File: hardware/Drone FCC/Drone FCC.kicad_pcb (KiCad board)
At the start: 2 copper layers, 137.2 x 68.6 mm, 24 parts, among them J1 Mag Dupont, J17 Conn_01x04, J18 Conn_01x04, J19 GPS M8N - DF13, J2 GPS Dupont, J20 Mag DF13, J21 Micro_SD_Card_Det_Hirose_DM3AT, J22 Conn_02x05_Odd_Even, J23 47589-0001, J24 DSM Spektrum JST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

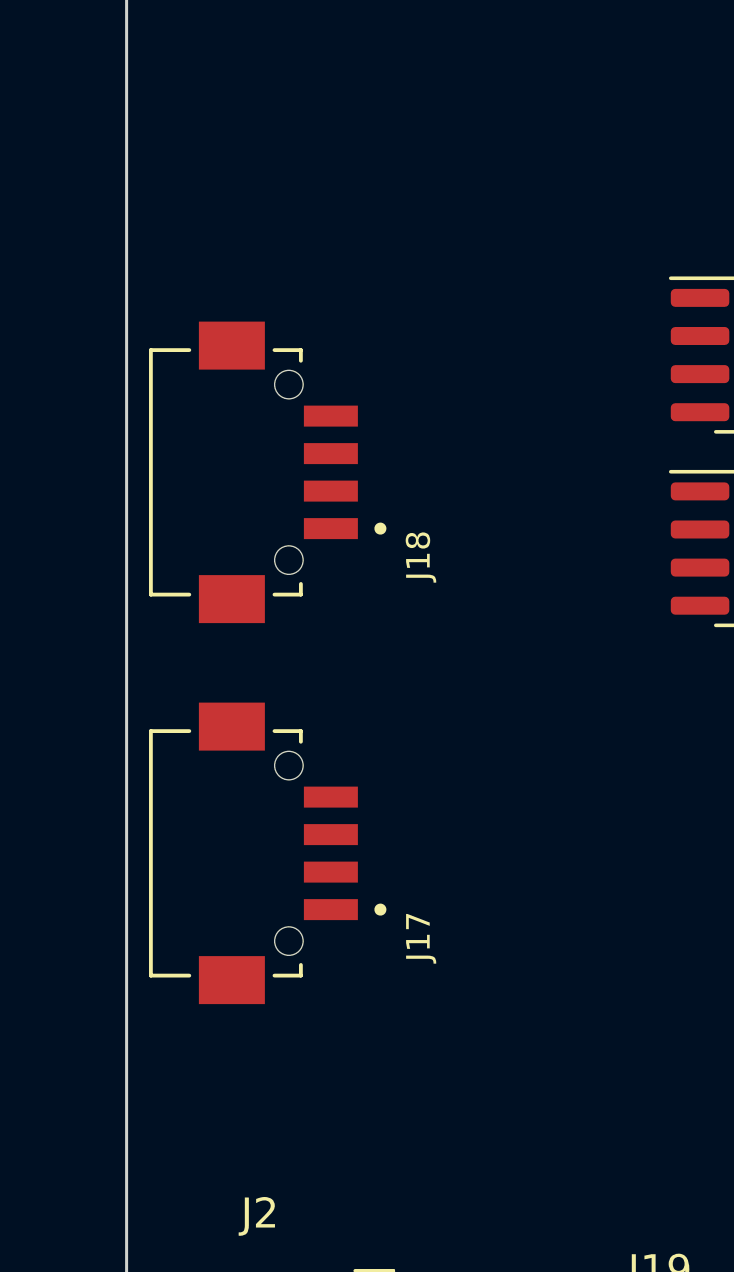
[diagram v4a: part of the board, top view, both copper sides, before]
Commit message: add functional schematic for microSD
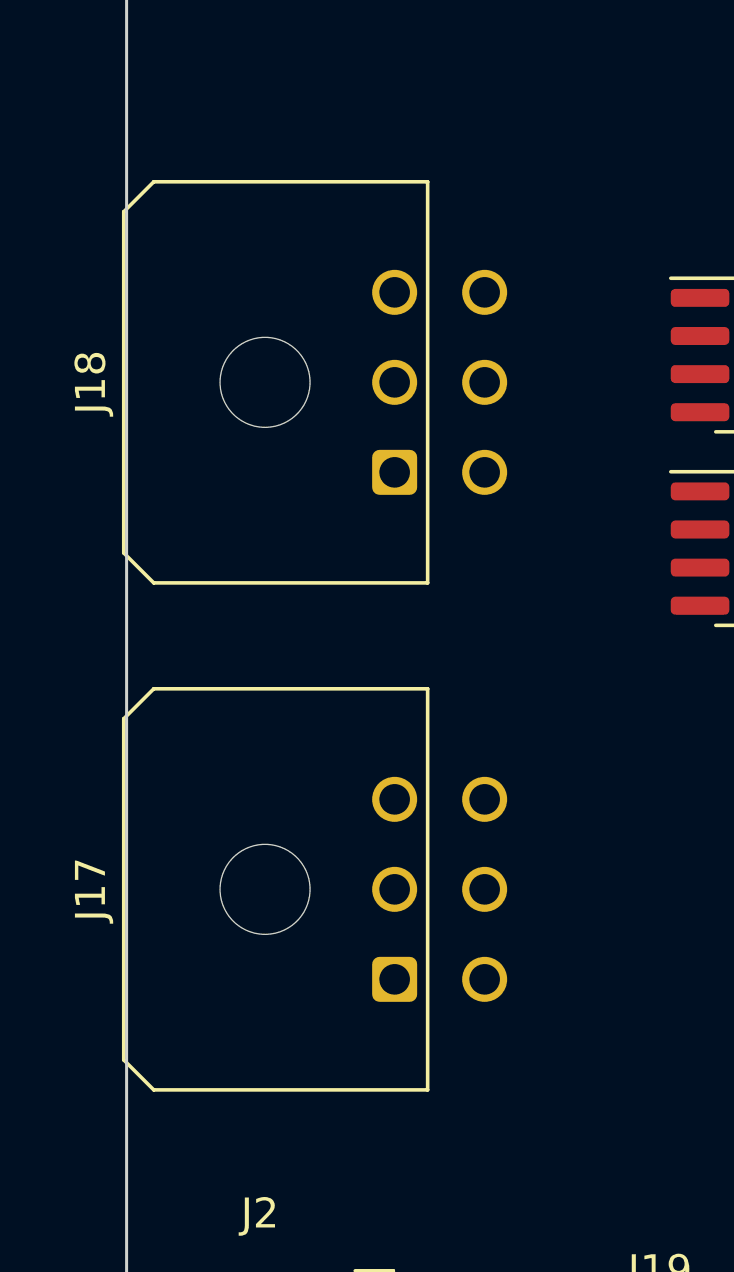
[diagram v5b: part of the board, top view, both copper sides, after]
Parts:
- J17: value Conn_01x04 -> CAN 1; footprint DF13-4P-1.25H:HRS_DF13-4P-1.25H(75) -> Connector_Molex:Molex_Micro-Fit_3.0_43045-0600_2x03_P3.00mm_Horizontal
- J18: value Conn_01x04 -> CAN 2; footprint DF13-4P-1.25H:HRS_DF13-4P-1.25H(75) -> Connector_Molex:Molex_Micro-Fit_3.0_43045-0600_2x03_P3.00mm_Horizontal
- moved J17 5.48 mm to (91.5, 82.9)
- moved J18 3.53 mm to (91.5, 66.0)
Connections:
- J17 pad 1: 5V -> unconnected-(J17-Pad1)
- J17 pad 4: GND -> unconnected-(J17-Pad4)
- J18 pad 1: 5V -> unconnected-(J18-Pad1)
- J18 pad 4: GND -> unconnected-(J18-Pad4)

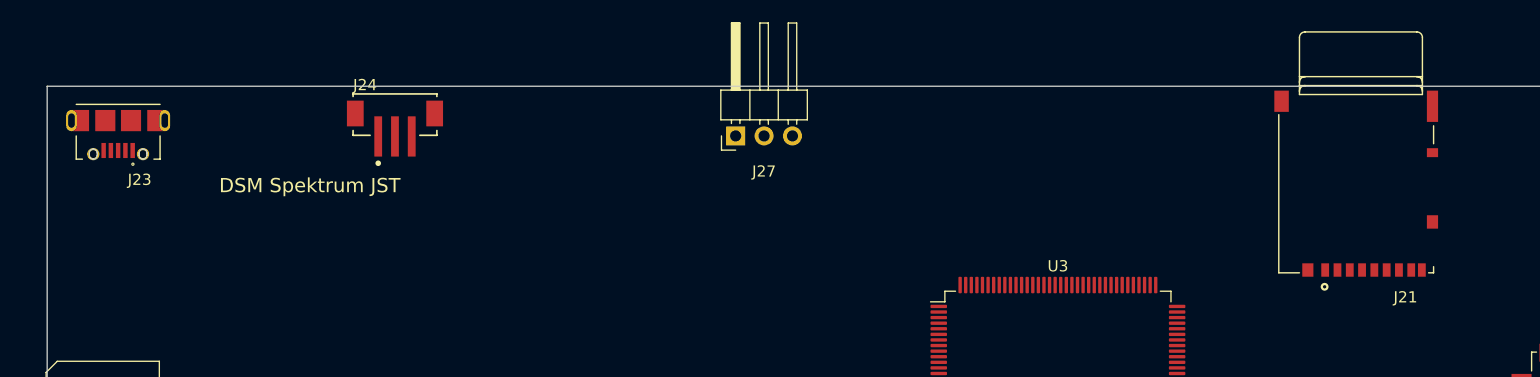
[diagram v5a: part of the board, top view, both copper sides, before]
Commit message: changed usb 2.0 AB connector for usb 2.0 B
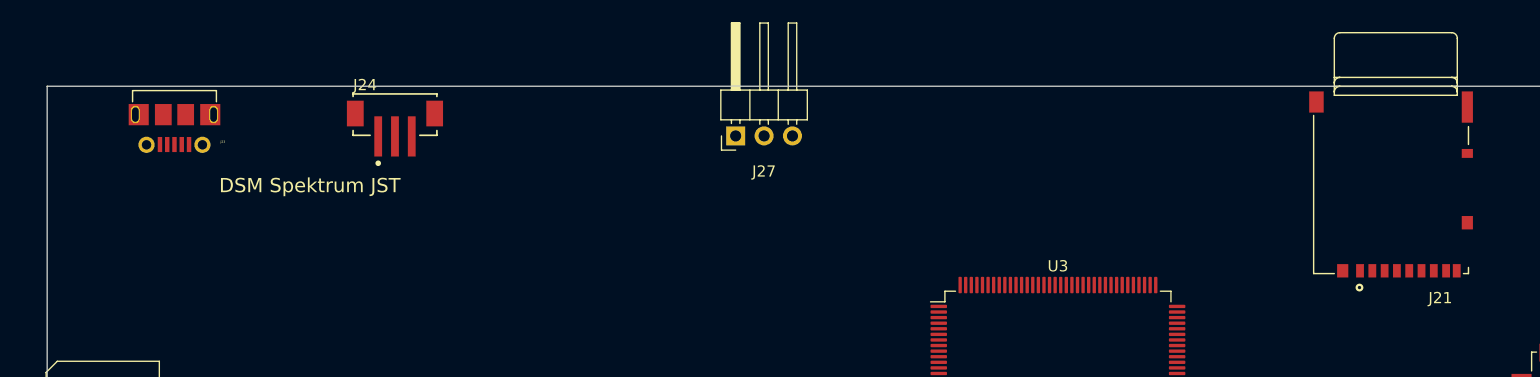
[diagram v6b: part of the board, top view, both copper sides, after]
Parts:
- J23: value 47589-0001 -> 105017-0001; footprint 47589-0001:MOLEX_47589-0001 -> 105017-0001:MOLEX_105017-0001
- moved J23 5.20 mm to (93.9, 34.3)
- moved J21 3.12 mm to (203.2, 48.3)
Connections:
- J21 pad 1: unconnected-(J21-Pad1) -> /MCU/SDMMC1_D2
- J21 pad 2: unconnected-(J21-Pad2) -> /MCU/SDMMC1_D3
- J21 pad 3: unconnected-(J21-Pad3) -> /MCU/SDMMC1_CMD
- J21 pad 5: unconnected-(J21-Pad5) -> /MCU/SDMMC1_CK
- J21 pad 7: unconnected-(J21-Pad7) -> /MCU/SDMMC1_D0
- J21 pad 8: unconnected-(J21-Pad8) -> /MCU/SDMMC1_D1
- U3 pad 111: unconnected-(U3-Pad111) -> /MCU/SDMMC1_D2
- U3 pad 112: unconnected-(U3-Pad112) -> /MCU/SDMMC1_D3
- U3 pad 113: unconnected-(U3-Pad113) -> /MCU/SDMMC1_CK
- U3 pad 116: unconnected-(U3-Pad116) -> /MCU/SDMMC1_CMD
- U3 pad 98: unconnected-(U3-Pad98) -> /MCU/SDMMC1_D0
- U3 pad 99: unconnected-(U3-Pad99) -> /MCU/SDMMC1_D1

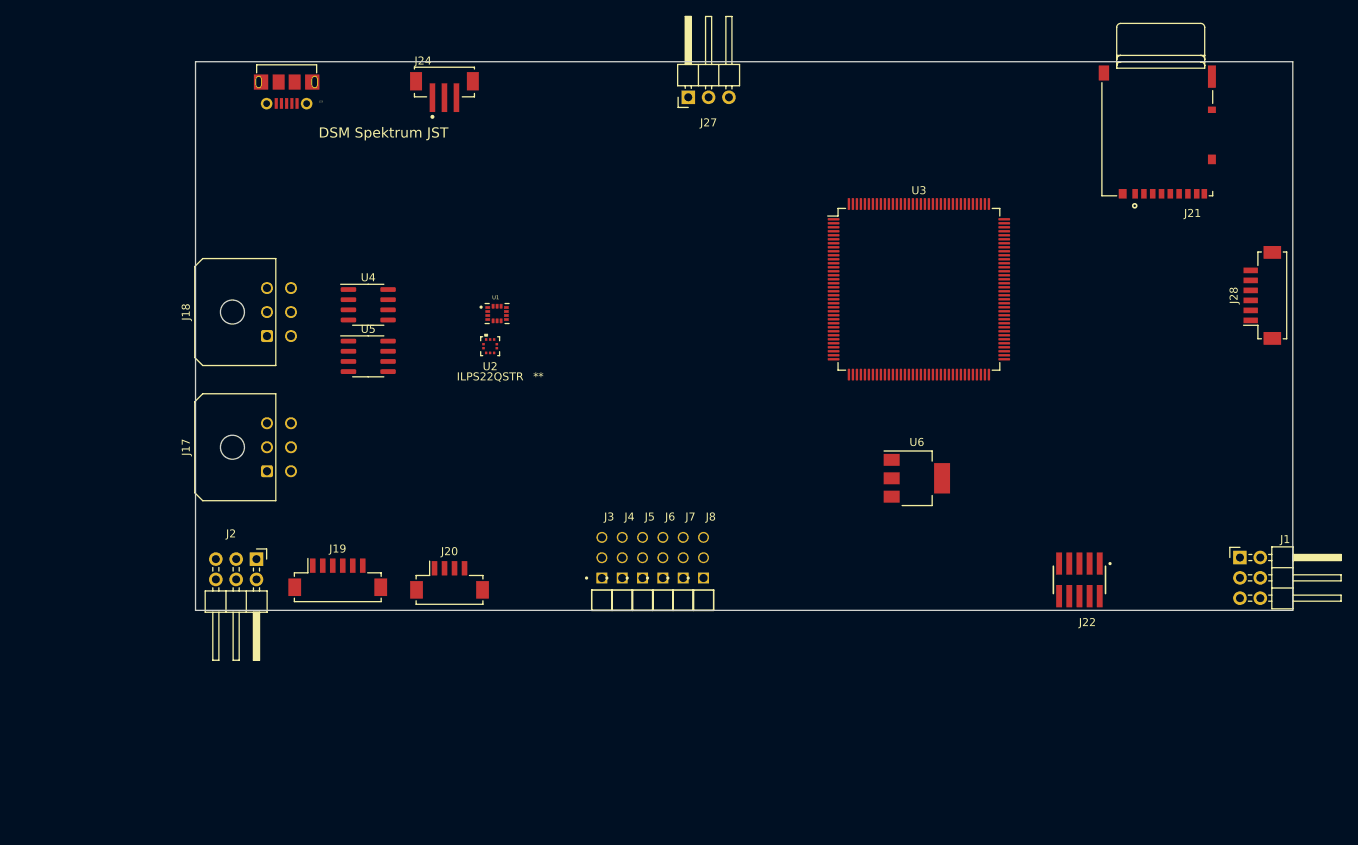
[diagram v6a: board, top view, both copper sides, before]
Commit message: add CAN schematic
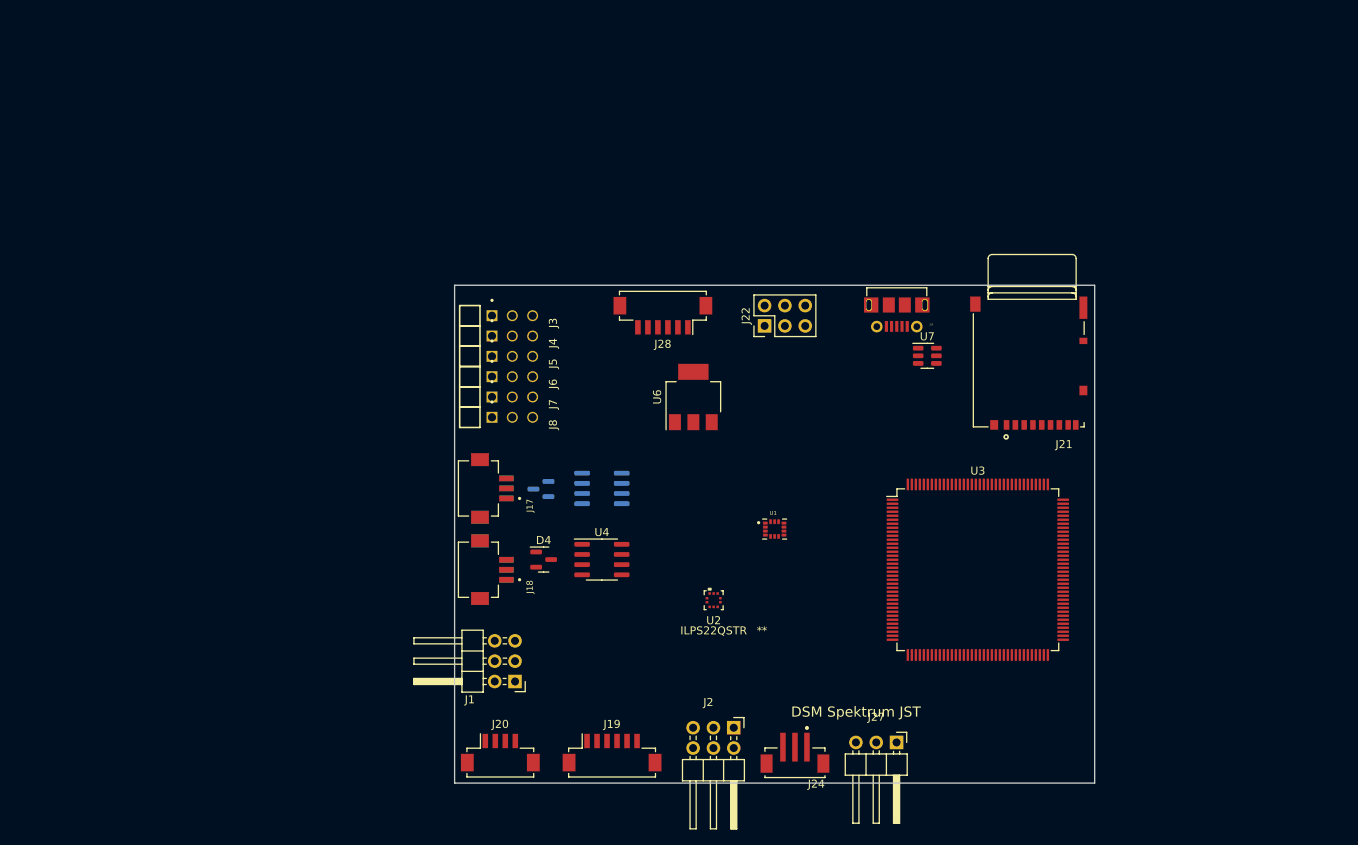
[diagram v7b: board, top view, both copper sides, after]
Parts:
- added D4: SM712_SOT23, Package_TO_SOT_SMD:SOT-23, F.Cu at (126.1, 94.0)
- added D5: SM712_SOT23, Package_TO_SOT_SMD:SOT-23, B.Cu at (125.7, 85.2)
- added J25: 105017-0001, 105017-0001:MOLEX_105017-0001, F.Cu at (170.2, 62.2)
- added J26: Conn_01x03, DF13A-3P-1.25H(21):HRS_DF13A-3P-1.25H(21), B.Cu at (118.1, 95.2)
- added U7: USBLC6-2SC6, Package_TO_SOT_SMD:SOT-23-6, F.Cu at (174.0, 68.5)
- J17: value CAN 1 -> Conn_01x03; footprint Connector_Molex:Molex_Micro-Fit_3.0_43045-0600_2x03_P3.00mm_Horizontal -> DF13A-3P-1.25H(21):HRS_DF13A-3P-1.25H(21)
- J18: value CAN 2 -> Conn_01x03; footprint Connector_Molex:Molex_Micro-Fit_3.0_43045-0600_2x03_P3.00mm_Horizontal -> DF13A-3P-1.25H(21):HRS_DF13A-3P-1.25H(21)
- J22: value Conn_02x05_Odd_Even -> Conn_02x03_Counter_Clockwise; footprint FTSH-105-01-F-DV-K-TR:SAMTEC_FTSH-105-01-F-DV-P-TR -> Connector_PinHeader_2.54mm:PinHeader_2x03_P2.54mm_Vertical
- J23: value 105017-0001 -> Conn_01x03; footprint 105017-0001:MOLEX_105017-0001 -> DF13A-3P-1.25H(21):HRS_DF13A-3P-1.25H(21); moved to B.Cu
- U5: moved to B.Cu
- moved J24 95.7 mm to (157.5, 119.4), turned to 180 degrees
- moved J1 91.9 mm to (122.5, 109.2), turned to 180 degrees
- moved J27 84.7 mm to (170.2, 116.8), turned to -90 degrees
- moved J28 75.0 mm to (141.0, 63.5), turned to 180 degrees
- moved J2 63.3 mm to (149.8, 115.0)
- moved J23 56.3 mm to (118.1, 85.1), turned to -90 degrees
- moved J22 50.6 mm to (153.7, 64.8), turned to 90 degrees
- moved U1 43.9 mm to (154.9, 90.2)
- moved U4 43.2 mm to (133.3, 94.0)
- moved U2 42.3 mm to (147.3, 99.1)
- moved J19 40.7 mm to (134.6, 118.1)
- moved J18 39.5 mm to (118.1, 95.2)
- moved J3 39.2 mm to (116.8, 63.5), turned to -90 degrees
- moved J4 38.1 mm to (116.8, 66.0), turned to -90 degrees
- moved J5 37.4 mm to (116.8, 68.6), turned to -90 degrees
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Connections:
- net /MCU/CAN1_RX renamed /Interfaz_CAN/CAN1_RX
- net /MCU/CAN1_TX renamed /Interfaz_CAN/CAN1_TX
- net /MCU/CAN2_RX renamed /Interfaz_CAN/CAN2_RX
- net /MCU/CAN2_TX renamed /Interfaz_CAN/CAN2_TX
- net /SPI1_MISO renamed /MCU/SPI1_MISO
- net /SPI1_MOSI renamed /MCU/SPI1_MOSI
- net /SPI1_SCK renamed /MCU/SPI1_SCK
- J1 pad 5: /I2C4_SCL -> /Sensores/MAG_SCL
- J1 pad 6: /I2C4_SDA -> /Sensores/MAG_SDA
- J17 pad 1: unconnected-(J17-Pad1) -> Net-(U4-Pad7)
- J17 pad 2: Net-(J17-Pad2) -> Net-(U4-Pad6)
- J17 pad 3: Net-(J17-Pad3) -> GND
- J18 pad 1: unconnected-(J18-Pad1) -> Net-(U4-Pad7)
- J18 pad 2: Net-(J18-Pad2) -> Net-(U4-Pad6)
- J18 pad 3: Net-(J18-Pad3) -> GND
- J19 pad 4: /USART1_RX -> /Sensores/GNSS_Rx
- J19 pad 5: /USART1_TX -> /Sensores/GNSS_Tx
- J2 pad 1: /USART1_TX -> /Sensores/GNSS_Tx
- J2 pad 2: /USART1_RX -> /Sensores/GNSS_Rx
- J20 pad 2: /I2C4_SCL -> /Sensores/MAG_SCL
- J20 pad 3: /I2C4_SDA -> /Sensores/MAG_SDA
- J22 pad 2: /Debug/SWDIO/TMS -> /Debug/SWCLK
- J22 pad 4: /Debug/SWDCLK/TCK -> /Debug/SWDIO
- J22 pad 5: GND -> /Debug/NRST
- J22 pad 6: /Debug/SWO/TDO -> /Debug/SWO
- J23 pad 1: unconnected-(J23-Pad1) -> Net-(D5-Pad1)
- J23 pad 2: unconnected-(J23-Pad2) -> Net-(D5-Pad2)
- J23 pad 3: unconnected-(J23-Pad3) -> GND
- J28 pad 3: unconnected-(J28-Pad3) -> Net-(C9-Pad1)
- J28 pad 4: unconnected-(J28-Pad4) -> Net-(C11-Pad1)
- J3 pad 1: /PWM1 -> /MCU/PWM1
- J4 pad 1: /PWM2 -> /MCU/PWM2
- J5 pad 1: /PWM3 -> /MCU/PWM3
- J6 pad 1: /PWM4 -> /MCU/PWM4
- J7 pad 1: /PWM5 -> /MCU/PWM8
- J8 pad 1: /PWM6 -> /MCU/PWM9
- U2 pad 2: /I2C2_SCL -> /MCU/I2C2_SCL
- U2 pad 4: /I2C2_SDA -> /MCU/I2C2_SDA
- U3 pad 101: /USART1_TX -> /MCU/OTG_FS_VBUS
- U3 pad 102: /USART1_RX -> /MCU/OTG_FS_ID
- U3 pad 103: unconnected-(U3-Pad103) -> /MCU/OTG_FS_DM
- U3 pad 104: unconnected-(U3-Pad104) -> /MCU/OTG_FS_DP
- U3 pad 105: unconnected-(U3-Pad105) -> /Debug/SWDIO
- U3 pad 109: unconnected-(U3-Pad109) -> /Debug/SWCLK
- U3 pad 133: unconnected-(U3-Pad133) -> /Debug/SWO
- U3 pad 23: unconnected-(U3-Pad23) -> /MCU/OSC_IN
- U3 pad 24: unconnected-(U3-Pad24) -> /MCU/OSC_OUT
- U3 pad 25: unconnected-(U3-Pad25) -> /Debug/NRST
- U3 pad 54: /I2C4_SDA -> /Sensores/MAG_SCL
- U3 pad 55: /I2C4_SCL -> /Sensores/MAG_SDA
- U3 pad 69: /I2C2_SDA -> /MCU/I2C2_SCL
- U3 pad 70: /I2C2_SCL -> /MCU/I2C2_SDA
- U3 pad 8: unconnected-(U3-Pad8) -> /MCU/OSC32_IN
- U3 pad 9: unconnected-(U3-Pad9) -> /MCU/OSC32_OUT
- U3 pad 95: unconnected-(U3-Pad95) -> /MCU/VDDUSB
- U4 pad 1: unconnected-(U4-Pad1) -> Net-(U4-Pad1)
- U4 pad 4: unconnected-(U4-Pad4) -> Net-(U4-Pad4)
- U4 pad 6: Net-(J17-Pad3) -> Net-(U4-Pad6)
- U4 pad 7: Net-(J17-Pad2) -> Net-(U4-Pad7)
- U4 pad 8: unconnected-(U4-Pad8) -> Net-(U4-Pad8)
- U5 pad 1: unconnected-(U5-Pad1) -> Net-(R24-Pad2)
- U5 pad 4: unconnected-(U5-Pad4) -> Net-(R21-Pad2)
- U5 pad 6: Net-(J18-Pad3) -> Net-(D5-Pad2)
- U5 pad 7: Net-(J18-Pad2) -> Net-(D5-Pad1)
- U5 pad 8: unconnected-(U5-Pad8) -> Net-(R25-Pad2)
- U6 pad 1: unconnected-(U6-Pad1) -> GND
- U6 pad 2: unconnected-(U6-Pad2) -> 3V3
- U6 pad 3: unconnected-(U6-Pad3) -> Net-(C13-Pad1)
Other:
- board size 137.2 x 68.6 mm -> 80 x 62.2 mm

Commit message: rearranged FCC schematic
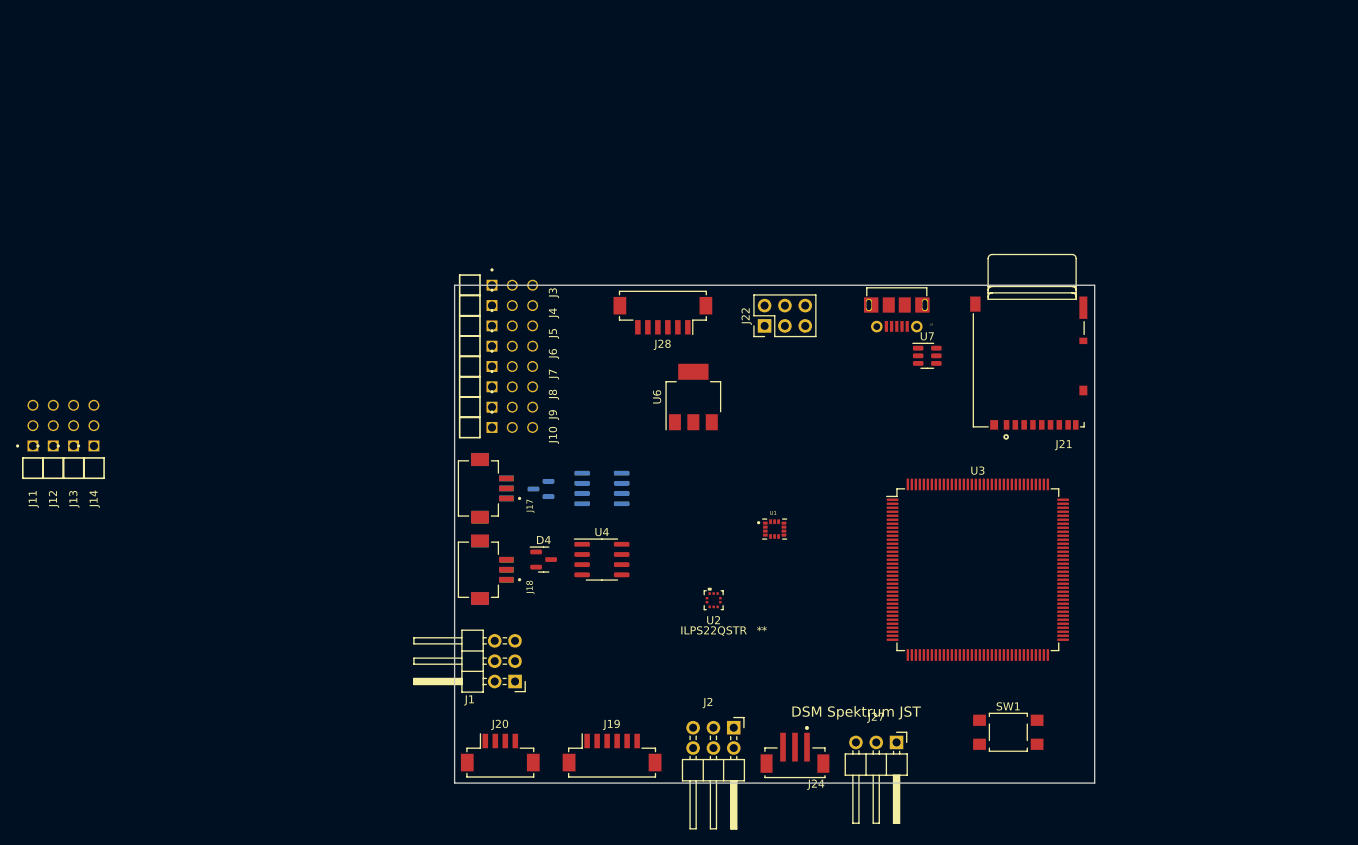
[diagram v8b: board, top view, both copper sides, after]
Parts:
- added J10: Conn_01x03, TSW-101-08-G-T-RA:SAMTEC_TSW-101-08-G-T-RA, F.Cu at (116.8, 77.5)
- added J11: Conn_01x03, TSW-101-08-G-T-RA:SAMTEC_TSW-101-08-G-T-RA, F.Cu at (62.2, 82.5)
- added J12: Conn_01x03, TSW-101-08-G-T-RA:SAMTEC_TSW-101-08-G-T-RA, F.Cu at (64.8, 82.5)
- added J13: Conn_01x03, TSW-101-08-G-T-RA:SAMTEC_TSW-101-08-G-T-RA, F.Cu at (67.3, 82.5)
- added J14: Conn_01x03, TSW-101-08-G-T-RA:SAMTEC_TSW-101-08-G-T-RA, F.Cu at (69.8, 82.5)
- added J9: Conn_01x03, TSW-101-08-G-T-RA:SAMTEC_TSW-101-08-G-T-RA, F.Cu at (116.8, 74.9)
- added SW1: SW_MEC_5E, Button_Switch_SMD:SW_SPST_TL3305A, F.Cu at (184.2, 115.6)
- moved J4 3.81 mm to (116.8, 62.2)
- moved J3 3.81 mm to (116.8, 59.7)
- moved J5 3.81 mm to (116.8, 64.8)
- moved J6 3.81 mm to (116.8, 67.3)
- moved J7 3.81 mm to (116.8, 69.8)
- moved J8 3.81 mm to (116.8, 72.4)
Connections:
- net /USB/VBUS renamed /Vbus
- J3 pad 2: 5V -> /Motores_servos_PWM/Vdd_motors
- J4 pad 2: 5V -> /Motores_servos_PWM/Vdd_motors
- J5 pad 2: 5V -> /Motores_servos_PWM/Vdd_motors
- J6 pad 2: 5V -> /Motores_servos_PWM/Vdd_motors
- J7 pad 2: 5V -> /Motores_servos_PWM/Vdd_motors
- J8 pad 2: 5V -> /Motores_servos_PWM/Vdd_motors
- U3 pad 106: unconnected-(U3-Pad106) -> /MCU/VCAP_2
- U3 pad 107: unconnected-(U3-Pad107) -> GND
- U3 pad 108: unconnected-(U3-Pad108) -> 3V3
- U3 pad 120: unconnected-(U3-Pad120) -> GND
- U3 pad 121: unconnected-(U3-Pad121) -> 3V3
- U3 pad 130: unconnected-(U3-Pad130) -> GND
- U3 pad 131: unconnected-(U3-Pad131) -> 3V3
- U3 pad 138: unconnected-(U3-Pad138) -> /MCU/BOOT0
- U3 pad 143: unconnected-(U3-Pad143) -> /MCU/PDR_ON
- U3 pad 144: unconnected-(U3-Pad144) -> 3V3
- U3 pad 16: unconnected-(U3-Pad16) -> GND
- U3 pad 17: unconnected-(U3-Pad17) -> 3V3
- U3 pad 30: unconnected-(U3-Pad30) -> 3V3
- U3 pad 31: unconnected-(U3-Pad31) -> GND
- U3 pad 32: unconnected-(U3-Pad32) -> 3V3
- U3 pad 33: unconnected-(U3-Pad33) -> 3V3
- U3 pad 38: unconnected-(U3-Pad38) -> GND
- U3 pad 39: unconnected-(U3-Pad39) -> 3V3
- U3 pad 51: unconnected-(U3-Pad51) -> GND
- U3 pad 52: unconnected-(U3-Pad52) -> 3V3
- U3 pad 6: unconnected-(U3-Pad6) -> 3V3
- U3 pad 61: unconnected-(U3-Pad61) -> GND
- U3 pad 62: unconnected-(U3-Pad62) -> 3V3
- U3 pad 7: unconnected-(U3-Pad7) -> /MCU/SD_SW
- U3 pad 71: unconnected-(U3-Pad71) -> /MCU/VCAP_1
- U3 pad 72: unconnected-(U3-Pad72) -> 3V3
- U3 pad 83: unconnected-(U3-Pad83) -> GND
- U3 pad 84: unconnected-(U3-Pad84) -> 3V3
- U3 pad 94: unconnected-(U3-Pad94) -> GND
- U3 pad 95: /MCU/VDDUSB -> 3V3
